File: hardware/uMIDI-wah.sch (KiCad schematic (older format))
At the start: 31 parts, among them IC1 TL072, SW1 MMP221, U1 Opamp_Dual_Generic, X1 AudioJack3_Switch, X2 Conn_01x08, X3 AudioJack3_Switch

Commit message: Create footprint for audio jacks
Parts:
- RV1, RV2, RV3: footprint (none) -> Potentiometer_THT:Potentiometer_Vishay_T7-YA_Single_Vertical
- X1, X3: footprint (none) -> umidi-wah:AudioJack 6.3mm Stereo; Manufacturer (none) -> RS; Manufacturer Part Number (none) -> -; Supplier (none) -> RS; Supplier Link (none) -> https://de.rs-online.com/web/p/klinkenstecker/9131037/; Supplier Part Number (none) -> 913-1037
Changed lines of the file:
@@
 F 0 "X1" H 2804 1392 50  0000 C CNN
 F 1 "AudioJack3_Switch" H 2804 1301 50  0000 C CNN
-F 2 "" H 2800 950 50  0001 C CNN
-F 3 "~" H 2800 950 50  0001 C CNN
+F 2 "umidi-wah:AudioJack 6.3mm Stereo" H 2800 950 50  0001 C CNN
+F 3 "https://docs-emea.rs-online.com/webdocs/14b5/0900766b814b516f.pdf" H 2800 950 50  0001 C CNN
+F 4 "RS" H 2804 1392 50  0001 C CNN "Supplier"
+F 5 "913-1037" H 2804 1392 50  0001 C CNN "Supplier Part Number"
+F 6 "https://de.rs-online.com/web/p/klinkenstecker/9131037/" H 2804 1392 50  0001 C CNN "Supplier Link"
+F 7 "RS" H 2804 1392 50  0001 C CNN "Manufacturer"
+F 8 "-" H 2804 1392 50  0001 C CNN "Manufacturer Part Number"
 	1    2800 950
 	1    0    0    -1
@@
 F 0 "X3" H 6167 971 50  0000 R CNN
 F 1 "AudioJack3_Switch" H 6167 880 50  0000 R CNN
-F 2 "" H 6400 950 50  0001 C CNN
-F 3 "~" H 6400 950 50  0001 C CNN
+F 2 "umidi-wah:AudioJack 6.3mm Stereo" H 6400 950 50  0001 C CNN
+F 3 "https://docs-emea.rs-online.com/webdocs/14b5/0900766b814b516f.pdf" H 6400 950 50  0001 C CNN
+F 4 "RS" H 6167 971 50  0001 R CNN "Supplier"
+F 5 "913-1037" H 6167 971 50  0001 R CNN "Supplier Part Number"
+F 6 "https://de.rs-online.com/web/p/klinkenstecker/9131037/" H 6167 971 50  0001 R CNN "Supplier Link"
+F 7 "RS" H 6167 971 50  0001 R CNN "Manufacturer"
+F 8 "-" H 6167 971 50  0001 R CNN "Manufacturer Part Number"
 	1    6400 950
 	-1   0    0    -1
@@
 F 0 "RV1" V 5550 3850 50  0000 R CNN
 F 1 "470k" V 5500 3850 50  0000 R CNN
-F 2 "" H 5250 3650 50  0001 C CNN
-F 3 "~" H 5250 3650 50  0001 C CNN
+F 2 "Potentiometer_THT:Potentiometer_Vishay_T7-YA_Single_Vertical" H 5250 3650 50  0001 C CNN
+F 3 "https://docs-emea.rs-online.com/webdocs/0021/0900766b8002111f.pdf" H 5250 3650 50  0001 C CNN
 F 4 "RS" V 5550 3850 50  0001 R CNN "Supplier"
 F 5 "374-6844" V 5550 3850 50  0001 R CNN "Supplier Part Number"
@@
 F 0 "RV3" V 7850 3650 50  0000 R CNN
 F 1 "470k" V 7800 3650 50  0000 R CNN
-F 2 "" H 7550 3450 50  0001 C CNN
-F 3 "~" H 7550 3450 50  0001 C CNN
+F 2 "Potentiometer_THT:Potentiometer_Vishay_T7-YA_Single_Vertical" H 7550 3450 50  0001 C CNN
+F 3 "https://docs-emea.rs-online.com/webdocs/0021/0900766b8002111f.pdf" H 7550 3450 50  0001 C CNN
 F 4 "RS" V 7850 3650 50  0001 R CNN "Supplier"
 F 5 "374-6844" V 7850 3650 50  0001 R CNN "Supplier Part Number"
@@
 F 0 "RV2" V 6600 3950 50  0000 R CNN
 F 1 "470k" V 6550 3950 50  0000 R CNN
-F 2 "" H 6300 3750 50  0001 C CNN
-F 3 "~" H 6300 3750 50  0001 C CNN
+F 2 "Potentiometer_THT:Potentiometer_Vishay_T7-YA_Single_Vertical" H 6300 3750 50  0001 C CNN
+F 3 "https://docs-emea.rs-online.com/webdocs/0021/0900766b8002111f.pdf" H 6300 3750 50  0001 C CNN
 F 4 "RS" V 6600 3950 50  0001 R CNN "Supplier"
 F 5 "374-6844" V 6600 3950 50  0001 R CNN "Supplier Part Number"

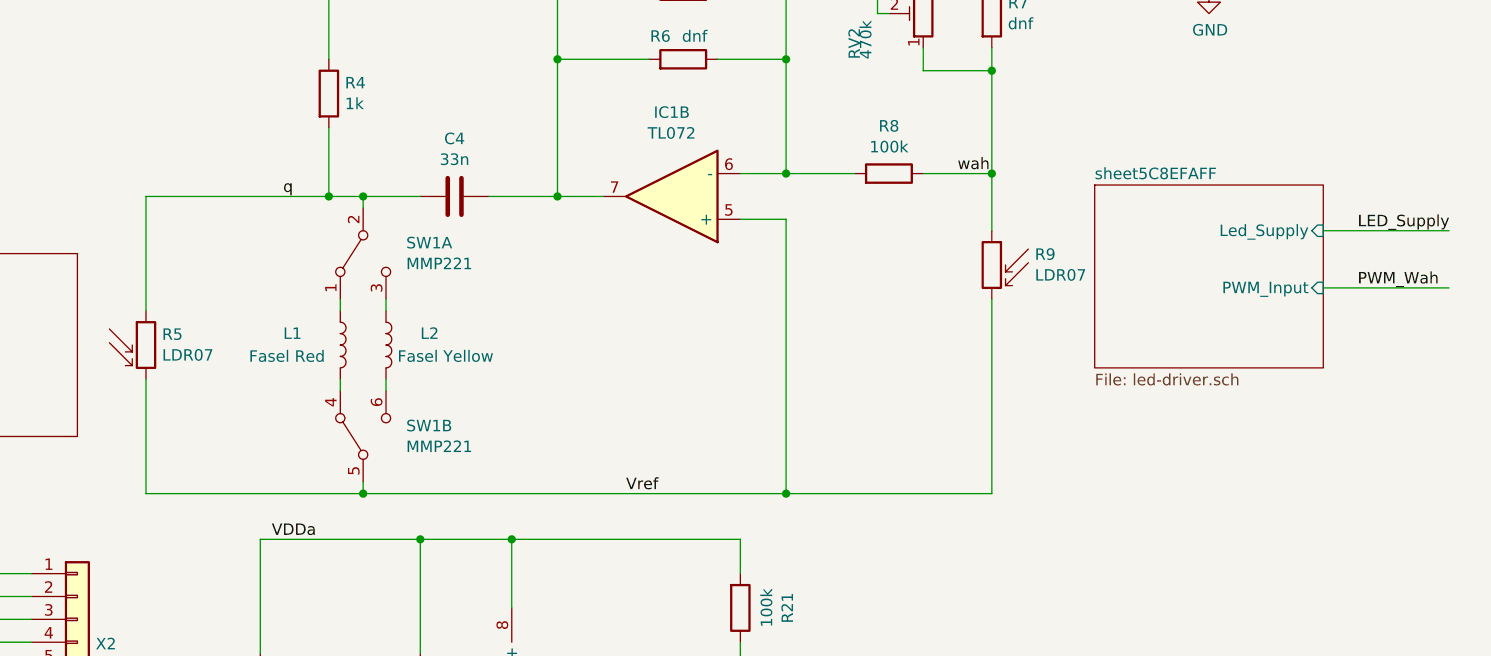
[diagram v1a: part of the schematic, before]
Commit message: Create footprint for LDRs
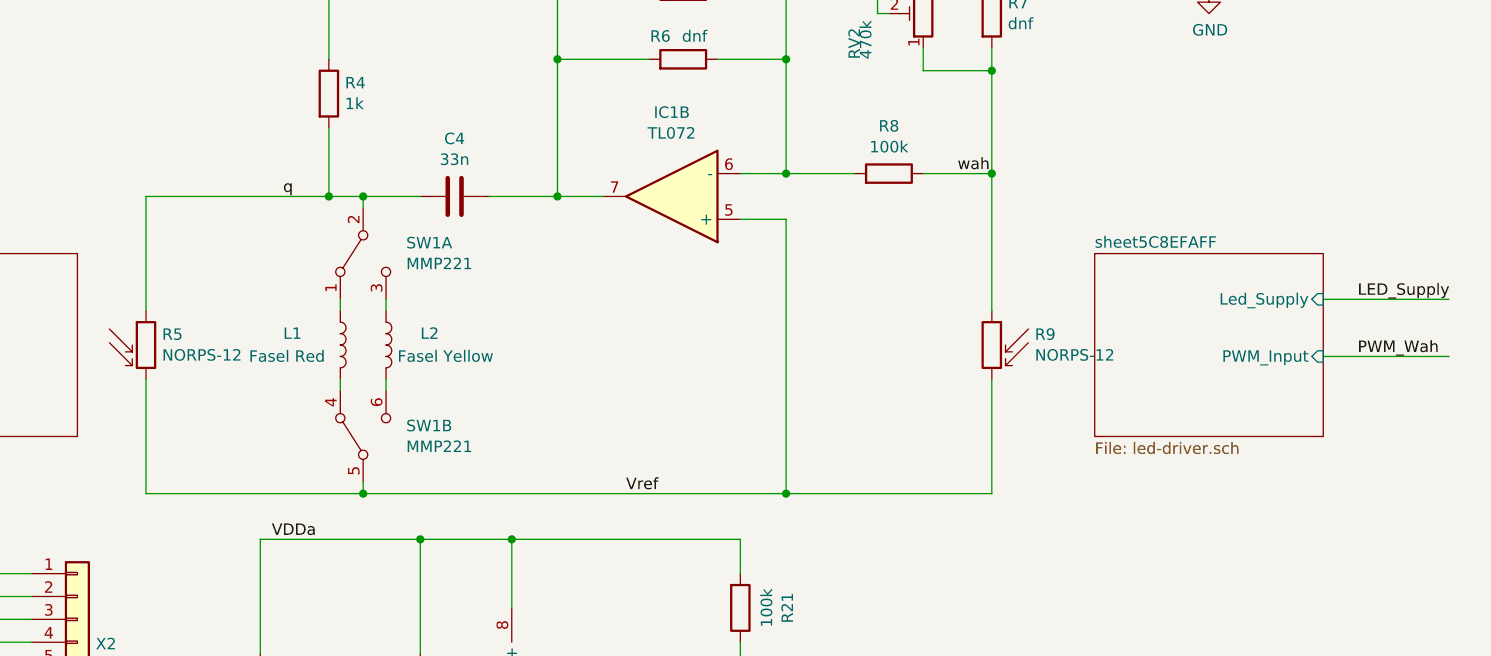
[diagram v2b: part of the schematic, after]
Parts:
- R5, R9: value LDR07 -> NORPS-12; footprint Resistors_SMD:R_0805 -> umidi-wah:LDR reverse mount; Manufacturer (none) -> Luna; Manufacturer Part Number (none) -> NORPS-12; Supplier (none) -> RS; Supplier Link (none) -> https://de.rs-online.com/web/p/fotowiderstande-ldr/9146714/; Supplier Part Number (none) -> 914-6714
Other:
- moved on the sheet: R9
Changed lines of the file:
@@
 P 2900 5200
 F 0 "R5" H 2970 5246 50  0000 L CNN
-F 1 "LDR07" H 2970 5155 50  0000 L CNN
-F 2 "Resistors_SMD:R_0805" V 3075 5200 50  0001 C CNN
-F 3 "" H 2900 5150 50  0001 C CNN
+F 1 "NORPS-12" H 2970 5155 50  0000 L CNN
+F 2 "umidi-wah:LDR reverse mount" V 3075 5200 50  0001 C CNN
+F 3 "https://docs-emea.rs-online.com/webdocs/1566/0900766b8156674b.pdf" H 2900 5150 50  0001 C CNN
+F 4 "RS" H 2970 5246 50  0001 L CNN "Supplier"
+F 5 "914-6714" H 2970 5246 50  0001 L CNN "Supplier Part Number"
+F 6 "https://de.rs-online.com/web/p/fotowiderstande-ldr/9146714/" H 2970 5246 50  0001 L CNN "Supplier Link"
+F 7 "Luna" H 2970 5246 50  0001 L CNN "Manufacturer"
+F 8 "NORPS-12" H 2970 5246 50  0001 L CNN "Manufacturer Part Number"
 	1    2900 5200
 	1    0    0    -1
@@
 L Sensor_Optical:LDR07 R9
 U 1 1 5C8C3558
-P 6600 4850
-F 0 "R9" H 6412 4896 50  0000 R CNN
-F 1 "LDR07" H 6412 4805 50  0000 R CNN
-F 2 "Resistors_SMD:R_0805" V 6775 4850 50  0001 C CNN
-F 3 "" H 6600 4800 50  0001 C CNN
-	1    6600 4850
+P 6600 5200
+F 0 "R9" H 6412 5246 50  0000 R CNN
+F 1 "NORPS-12" H 6412 5155 50  0000 R CNN
+F 2 "umidi-wah:LDR reverse mount" V 6775 5200 50  0001 C CNN
+F 3 "https://docs-emea.rs-online.com/webdocs/1566/0900766b8156674b.pdf" H 6600 5150 50  0001 C CNN
+F 4 "RS" H 6412 5246 50  0001 R CNN "Supplier"
+F 5 "914-6714" H 6412 5246 50  0001 R CNN "Supplier Part Number"
+F 6 "https://de.rs-online.com/web/p/fotowiderstande-ldr/9146714/" H 6412 5246 50  0001 R CNN "Supplier Link"
+F 7 "Luna" H 6412 5246 50  0001 R CNN "Manufacturer"
+F 8 "NORPS-12" H 6412 5246 50  0001 R CNN "Manufacturer Part Number"
+	1    6600 5200
 	-1   0    0    -1
 $EndComp
@@
 	2900 4550 3700 4550
 Wire Wire Line
-	6600 4700 6600 4450
+	6600 5050 6600 4450
 Connection ~ 6600 4450
 $Comp
@@
 $EndSheet
 $Sheet
-S 7050 4500 1000 800
+S 7050 4800 1000 800
 U 5C8EFAFF
 F0 "sheet5C8EFAFF" 50
 F1 "led-driver.sch" 50
-F2 "Led_Supply" I R 8050 4700 50
-F3 "PWM_Input" I R 8050 4950 50
+F2 "Led_Supply" I R 8050 5000 50
+F3 "PWM_Input" I R 8050 5250 50
 $EndSheet
 Wire Wire Line
@@
 PWM_Q
 Wire Wire Line
-	8050 4950 8600 4950
-Wire Wire Line
-	8050 4700 8600 4700
-Text Label 8200 4700 0    50   ~ 0
+	8050 5250 8600 5250
+Wire Wire Line
+	8050 5000 8600 5000
+Text Label 8200 5000 0    50   ~ 0
 LED_Supply
-Text Label 8200 4950 0    50   ~ 0
+Text Label 8200 5250 0    50   ~ 0
 PWM_Wah
 Wire Wire Line
@@
 Vref
 Wire Wire Line
-	6600 5000 6600 5850
+	6600 5350 6600 5850
 Wire Wire Line
 	2900 5350 2900 5850

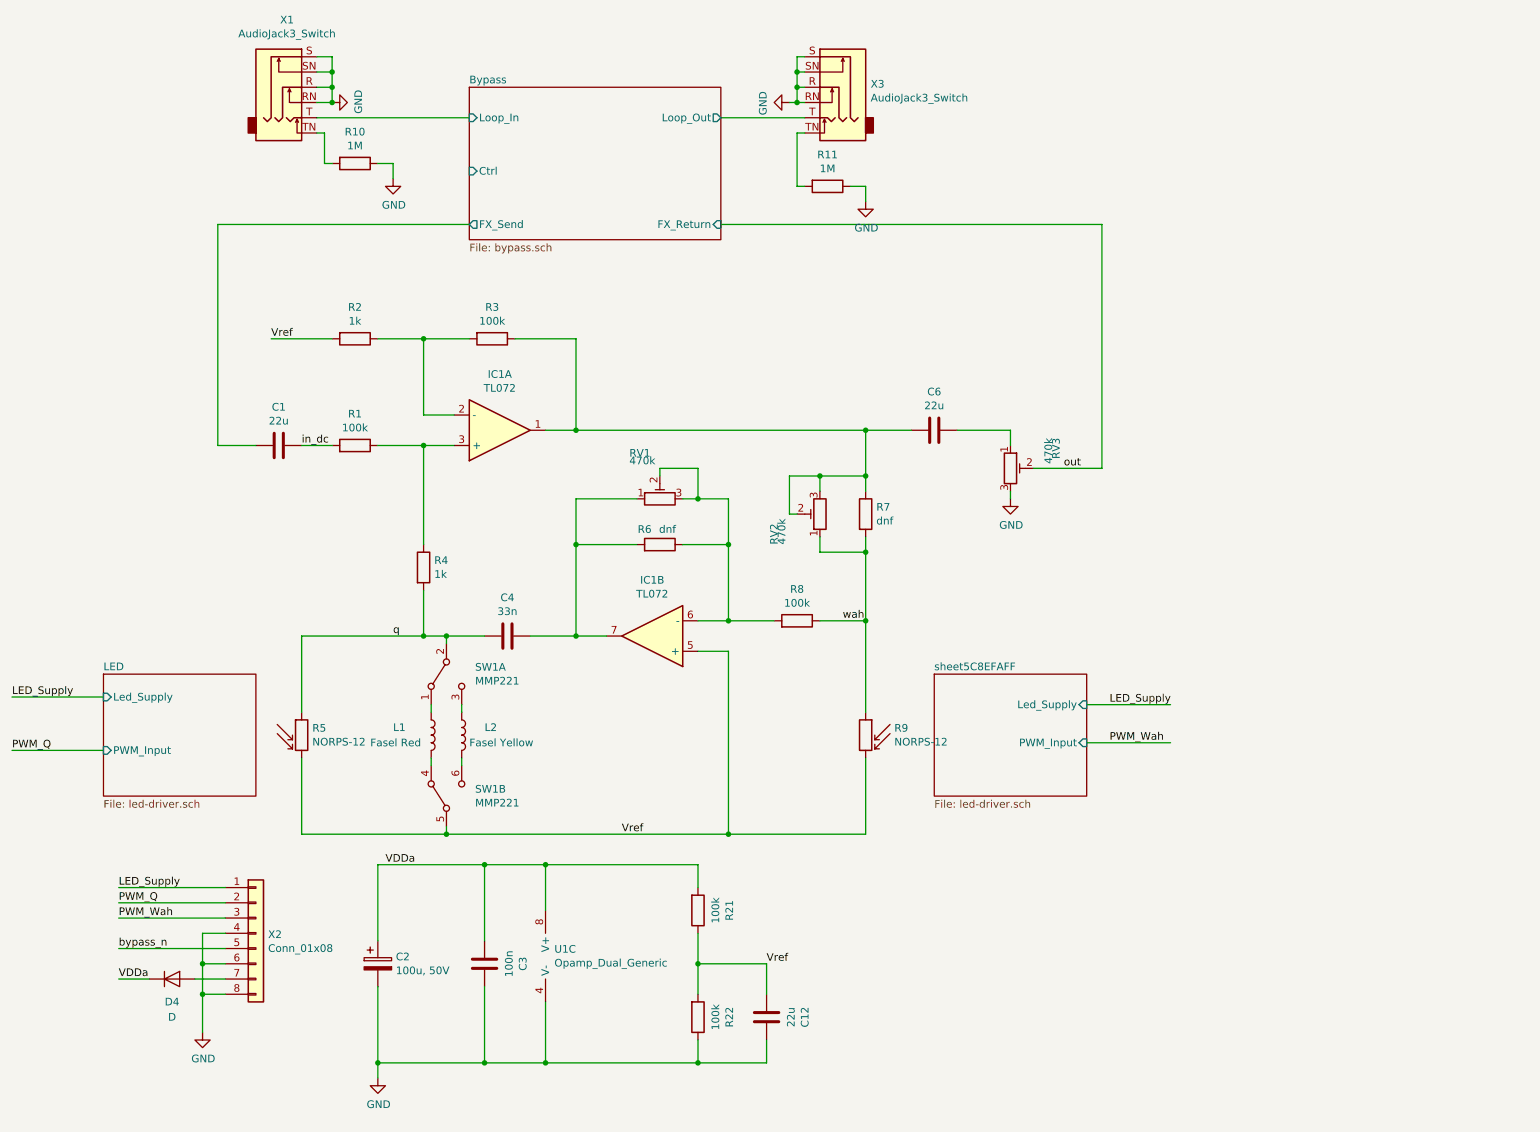
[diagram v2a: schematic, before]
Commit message: Assign footprints; add led supply circuit
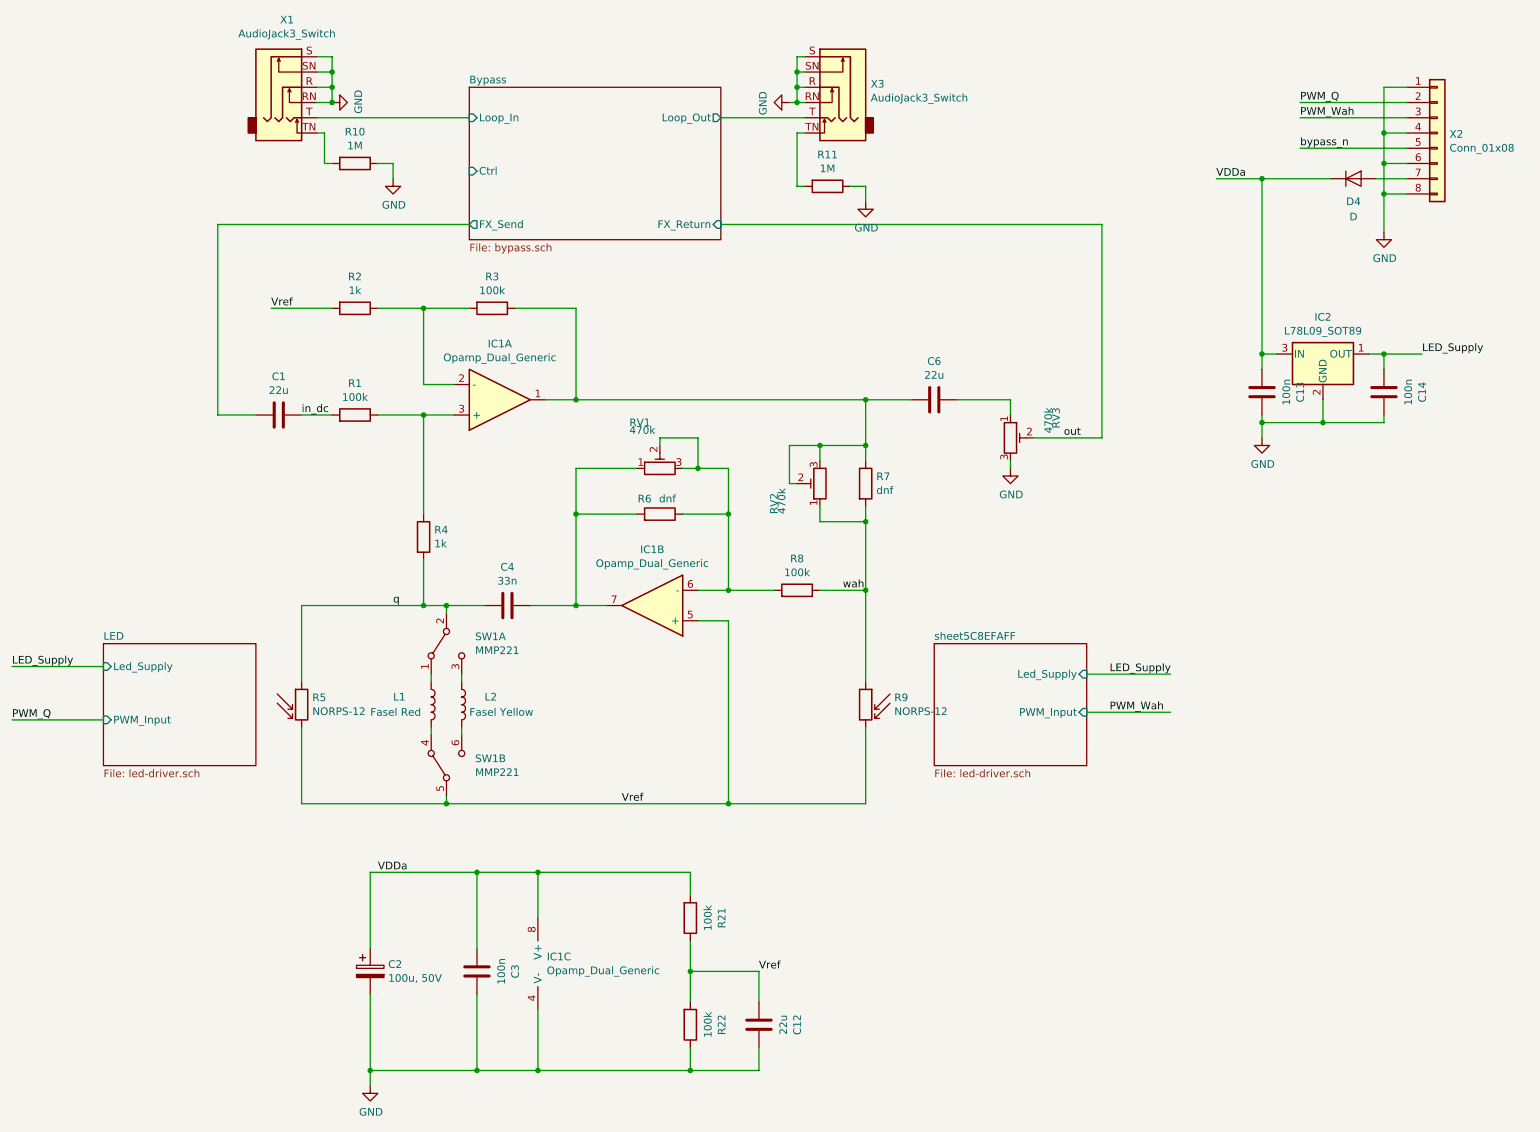
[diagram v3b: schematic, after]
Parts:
- added C13, C14: 100n, Capacitors_SMD:C_0805, symbol Device:C
- added IC2: L78L09_SOT89, Package_TO_SOT_SMD:SOT-89-3, symbol Regulator_Linear:L78L09_SOT89
- IC1: value TL072 -> Opamp_Dual_Generic; footprint Package_DIP:DIP-8_W7.62mm -> Package_DIP:DIP-8_W7.62mm_Socket_LongPads
- IC1: renamed from U1; footprint (none) -> Package_DIP:DIP-8_W7.62mm_Socket_LongPads; Manufacturer (none) -> TI; Manufacturer Part Number (none) -> TL072CP; Supplier (none) -> RS; Supplier Link (none) -> https://de.rs-online.com/web/p/operationsverstarker/0304239/; Supplier Part Number (none) -> 304-239
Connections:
- net GND: now also X2.1 (Pin_1), C13.1, C14.1, IC2.2 (GND)
- net LED_Supply: now also C14.2, IC2.1 (OUT); no longer X2.1 (Pin_1)
- net VDDa: now also C13.2, IC2.3 (IN)
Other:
- moved on the sheet: C1, C12, C2, C3, C4, C6, D4, IC1A, IC1B, IC1C, L1, L2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
